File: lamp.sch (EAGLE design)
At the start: 3 parts

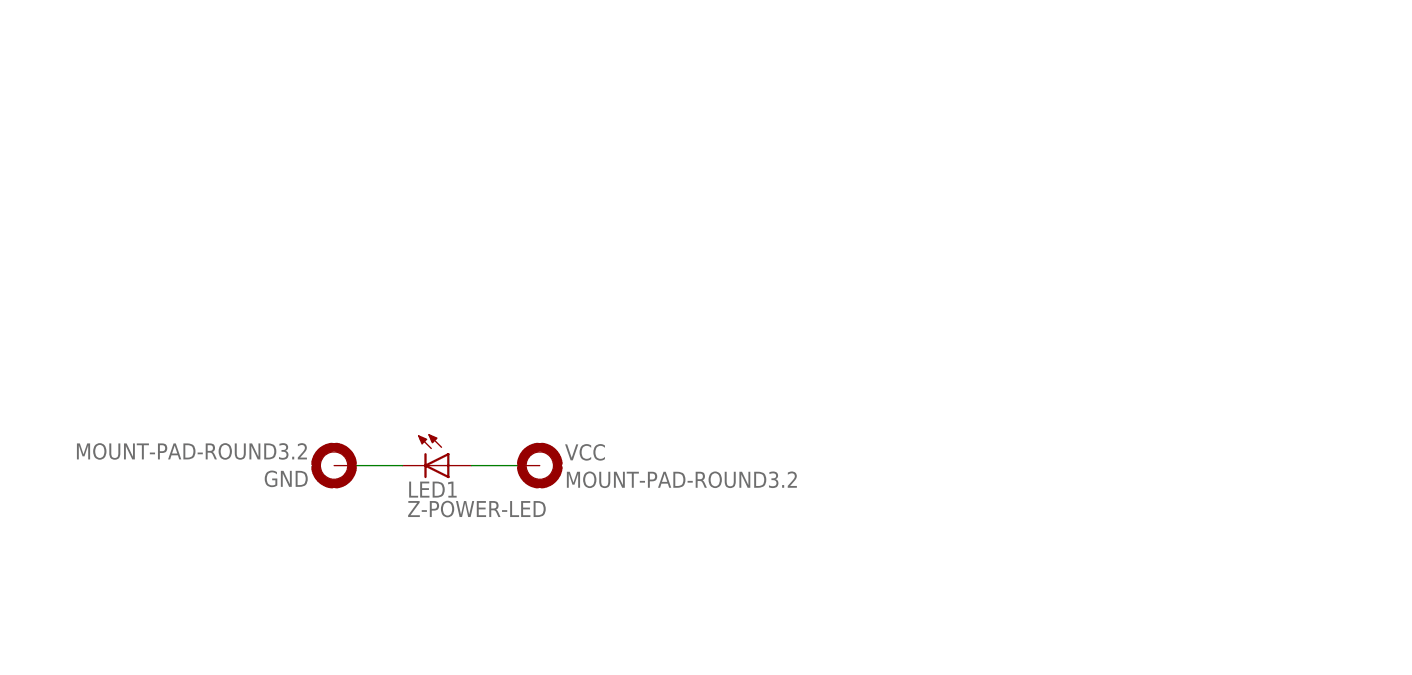
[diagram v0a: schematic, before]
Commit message: Updated the LED lamp schematic.
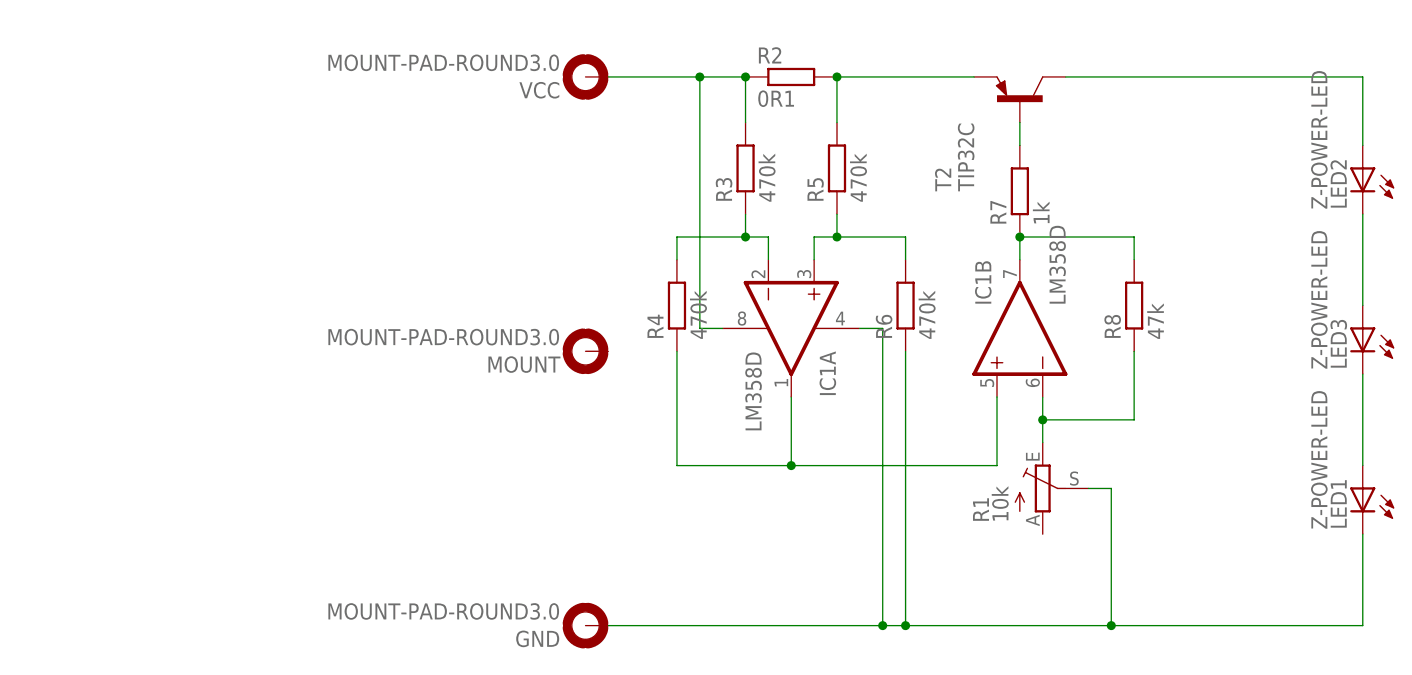
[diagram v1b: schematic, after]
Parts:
- added IC1: LM358D, linear:LM358D
- added LED2, LED3: Z-POWER-LED, led:Z-POWER-LED
- added MOUNT: MOUNT-PAD-ROUND3.0, holes:MOUNT-PAD-ROUND3.0
- added R1: 10k, pot:TRIM_EU-RJ9W
- added R2: 0R1, resistor:R-EU_0411/15
- added R3, R4, R5, R6: 470k, resistor:R-EU_M1206
- added R7: 1k, resistor:R-EU_M1206
- added R8: 47k, resistor:R-EU_M1206
- added T2: TIP32C, transistor:TIP32C
- GND, VCC: value MOUNT-PAD-ROUND3.2 -> MOUNT-PAD-ROUND3.0; device holes:MOUNT-PAD-ROUND3.2 -> holes:MOUNT-PAD-ROUND3.0
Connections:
- removed net N$1: GND.MOUNT, LED1.C
- new net GND: GND.MOUNT, IC1P.V-, LED1.C, R1.S, R6.1
- new net N$10: IC1B.-IN, R1.E, R8.1
- new net N$11: IC1A.-IN, R3.1, R4.2
- new net N$12: IC1A.+IN, R5.1, R6.2
- new net N$3: R7.2, T2.B
- new net N$4: IC1B.OUT, R7.1, R8.2
- new net N$5: LED2.A, T2.C
- new net N$6: LED2.C, LED3.A
- new net N$7: LED1.A, LED3.C
- new net N$9: IC1A.OUT, IC1B.+IN, R4.1
- new net VCC: IC1P.V+, R2.1, R3.2, VCC.MOUNT
- net N$2: now also R2.2, R5.2, T2.E; no longer LED1.A, VCC.MOUNT
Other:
- moved on the sheet: GND, LED1, VCC

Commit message: Whoops...
Swapped pins in the schematic, so gotta redo the entire PCB layout.
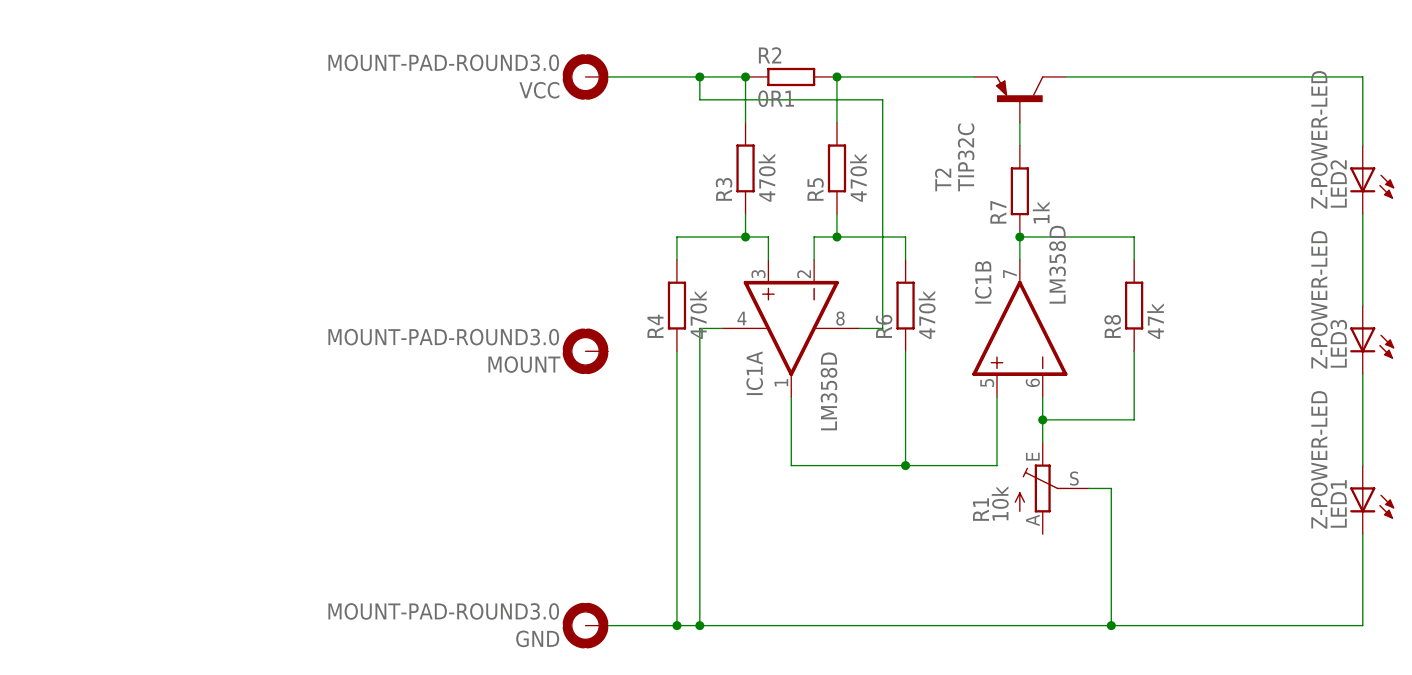
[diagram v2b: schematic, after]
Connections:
- net GND: now also R4.1; no longer R6.1
- net N$11: now also IC1A.+IN; no longer IC1A.-IN
- net N$12: now also IC1A.-IN; no longer IC1A.+IN
- net N$9: now also R6.1; no longer R4.1
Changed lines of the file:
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@@
 <grid distance="0.1" unitdist="inch" unit="inch" style="lines" multiple="1" display="no" altdistance="0.01" altunitdist="inch" altunit="inch"/>
 <layers>
-<layer number="1" name="Top" color="4" fill="1" visible="yes" active="no"/>
-<layer number="16" name="Bottom" color="1" fill="1" visible="yes" active="no"/>
-<layer number="17" name="Pads" color="2" fill="1" visible="yes" active="no"/>
-<layer number="18" name="Vias" color="2" fill="1" visible="yes" active="no"/>
-<layer number="19" name="Unrouted" color="6" fill="1" visible="yes" active="no"/>
-<layer number="20" name="Dimension" color="15" fill="1" visible="yes" active="no"/>
-<layer number="21" name="tPlace" color="7" fill="1" visible="yes" active="no"/>
-<layer number="22" name="bPlace" color="7" fill="1" visible="yes" active="no"/>
-<layer number="23" name="tOrigins" color="15" fill="1" visible="yes" active="no"/>
-<layer number="24" name="bOrigins" color="15" fill="1" visible="yes" active="no"/>
-<layer number="25" name="tNames" color="7" fill="1" visible="yes" active="no"/>
-<layer number="26" name="bNames" color="7" fill="1" visible="yes" active="no"/>
-<layer number="27" name="tValues" color="7" fill="1" visible="yes" active="no"/>
-<layer number="28" name="bValues" color="7" fill="1" visible="yes" active="no"/>
+<layer number="1" name="Top" color="4" fill="1" visible="no" active="no"/>
+<layer number="16" name="Bottom" color="1" fill="1" visible="no" active="no"/>
+<layer number="17" name="Pads" color="2" fill="1" visible="no" active="no"/>
+<layer number="18" name="Vias" color="2" fill="1" visible="no" active="no"/>
+<layer number="19" name="Unrouted" color="6" fill="1" visible="no" active="no"/>
+<layer number="20" name="Dimension" color="15" fill="1" visible="no" active="no"/>
+<layer number="21" name="tPlace" color="7" fill="1" visible="no" active="no"/>
+<layer number="22" name="bPlace" color="7" fill="1" visible="no" active="no"/>
+<layer number="23" name="tOrigins" color="15" fill="1" visible="no" active="no"/>
+<layer number="24" name="bOrigins" color="15" fill="1" visible="no" active="no"/>
+<layer number="25" name="tNames" color="7" fill="1" visible="no" active="no"/>
+<layer number="26" name="bNames" color="7" fill="1" visible="no" active="no"/>
+<layer number="27" name="tValues" color="7" fill="1" visible="no" active="no"/>
+<layer number="28" name="bValues" color="7" fill="1" visible="no" active="no"/>
 <layer number="29" name="tStop" color="7" fill="3" visible="no" active="no"/>
 <layer number="30" name="bStop" color="7" fill="6" visible="no" active="no"/>
@@
 <layer number="35" name="tGlue" color="7" fill="4" visible="no" active="no"/>
 <layer number="36" name="bGlue" color="7" fill="5" visible="no" active="no"/>
-<layer number="37" name="tTest" color="7" fill="1" visible="yes" active="no"/>
-<layer number="38" name="bTest" color="7" fill="1" visible="yes" active="no"/>
+<layer number="37" name="tTest" color="7" fill="1" visible="no" active="no"/>
+<layer number="38" name="bTest" color="7" fill="1" visible="no" active="no"/>
 <layer number="39" name="tKeepout" color="4" fill="11" visible="no" active="no"/>
 <layer number="40" name="bKeepout" color="1" fill="11" visible="no" active="no"/>
@@
 <layer number="44" name="Drills" color="7" fill="1" visible="no" active="no"/>
 <layer number="45" name="Holes" color="7" fill="1" visible="no" active="no"/>
-<layer number="46" name="Milling" color="3" fill="1" visible="yes" active="no"/>
-<layer number="47" name="Measures" color="7" fill="1" visible="yes" active="no"/>
-<layer number="48" name="Document" color="7" fill="1" visible="yes" active="no"/>
-<layer number="49" name="Reference" color="7" fill="1" visible="yes" active="no"/>
-<layer number="51" name="tDocu" color="7" fill="1" visible="yes" active="no"/>
-<layer number="52" name="bDocu" color="7" fill="1" visible="yes" active="no"/>
+<layer number="46" name="Milling" color="3" fill="1" visible="no" active="no"/>
+<layer number="47" name="Measures" color="7" fill="1" visible="no" active="no"/>
+<layer number="48" name="Document" color="7" fill="1" visible="no" active="no"/>
+<layer number="49" name="Reference" color="7" fill="1" visible="no" active="no"/>
+<layer number="51" name="tDocu" color="7" fill="1" visible="no" active="no"/>
+<layer number="52" name="bDocu" color="7" fill="1" visible="no" active="no"/>
 <layer number="91" name="Nets" color="2" fill="1" visible="yes" active="yes"/>
 <layer number="92" name="Busses" color="1" fill="1" visible="yes" active="yes"/>
@@
 <instances>
 <instance part="LED1" gate="G$1" x="81.28" y="48.26" rot="MR0"/>
-<instance part="IC1" gate="A" x="17.78" y="66.04" rot="R270"/>
+<instance part="IC1" gate="A" x="17.78" y="66.04" rot="MR270"/>
 <instance part="IC1" gate="B" x="43.18" y="66.04" rot="R90"/>
 <instance part="R1" gate="1" x="45.72" y="48.26"/>
@@
 <instance part="GND" gate="G$1" x="-5.08" y="33.02" rot="R180"/>
 <instance part="MOUNT" gate="G$1" x="-5.08" y="63.5" rot="R180"/>
-<instance part="IC1" gate="P" x="17.78" y="66.04" rot="R90"/>
+<instance part="IC1" gate="P" x="17.78" y="66.04" rot="MR90"/>
 </instances>
 <busses>
@@
 <wire x1="12.7" y1="93.98" x2="12.7" y2="88.9" width="0.1524" layer="91"/>
 <junction x="12.7" y="93.98"/>
-<wire x1="7.62" y1="93.98" x2="7.62" y2="66.04" width="0.1524" layer="91"/>
 <pinref part="IC1" gate="P" pin="V+"/>
-<wire x1="7.62" y1="66.04" x2="10.16" y2="66.04" width="0.1524" layer="91"/>
+<wire x1="25.4" y1="66.04" x2="27.94" y2="66.04" width="0.1524" layer="91"/>
+<wire x1="27.94" y1="66.04" x2="27.94" y2="91.44" width="0.1524" layer="91"/>
+<wire x1="27.94" y1="91.44" x2="7.62" y2="91.44" width="0.1524" layer="91"/>
+<wire x1="7.62" y1="91.44" x2="7.62" y2="93.98" width="0.1524" layer="91"/>
 <junction x="7.62" y="93.98"/>
 </segment>
@@
 <pinref part="GND" gate="G$1" pin="MOUNT"/>
 <pinref part="R1" gate="1" pin="S"/>
-<wire x1="53.34" y1="33.02" x2="30.48" y2="33.02" width="0.1524" layer="91"/>
-<wire x1="30.48" y1="33.02" x2="27.94" y2="33.02" width="0.1524" layer="91"/>
-<wire x1="27.94" y1="33.02" x2="-2.54" y2="33.02" width="0.1524" layer="91"/>
+<wire x1="53.34" y1="33.02" x2="7.62" y2="33.02" width="0.1524" layer="91"/>
+<wire x1="7.62" y1="33.02" x2="5.08" y2="33.02" width="0.1524" layer="91"/>
+<wire x1="5.08" y1="33.02" x2="-2.54" y2="33.02" width="0.1524" layer="91"/>
 <wire x1="50.8" y1="48.26" x2="53.34" y2="48.26" width="0.1524" layer="91"/>
 <wire x1="53.34" y1="48.26" x2="53.34" y2="33.02" width="0.1524" layer="91"/>
-<pinref part="R6" gate="G$1" pin="1"/>
-<wire x1="30.48" y1="63.5" x2="30.48" y2="33.02" width="0.1524" layer="91"/>
 <junction x="53.34" y="33.02"/>
-<junction x="30.48" y="33.02"/>
 <pinref part="IC1" gate="P" pin="V-"/>
-<wire x1="25.4" y1="66.04" x2="27.94" y2="66.04" width="0.1524" layer="91"/>
-<wire x1="27.94" y1="66.04" x2="27.94" y2="33.02" width="0.1524" layer="91"/>
-<junction x="27.94" y="33.02"/>
+<wire x1="10.16" y1="66.04" x2="7.62" y2="66.04" width="0.1524" layer="91"/>
+<wire x1="7.62" y1="66.04" x2="7.62" y2="33.02" width="0.1524" layer="91"/>
+<junction x="7.62" y="33.02"/>
+<pinref part="R4" gate="G$1" pin="1"/>
+<wire x1="5.08" y1="63.5" x2="5.08" y2="33.02" width="0.1524" layer="91"/>
+<junction x="5.08" y="33.02"/>
 </segment>
 </net>
@@
 <wire x1="17.78" y1="58.42" x2="17.78" y2="50.8" width="0.1524" layer="91"/>
 <pinref part="IC1" gate="B" pin="+IN"/>
-<wire x1="17.78" y1="50.8" x2="40.64" y2="50.8" width="0.1524" layer="91"/>
+<wire x1="17.78" y1="50.8" x2="30.48" y2="50.8" width="0.1524" layer="91"/>
+<wire x1="30.48" y1="50.8" x2="40.64" y2="50.8" width="0.1524" layer="91"/>
 <wire x1="40.64" y1="50.8" x2="40.64" y2="58.42" width="0.1524" layer="91"/>
-<pinref part="R4" gate="G$1" pin="1"/>
-<wire x1="5.08" y1="63.5" x2="5.08" y2="50.8" width="0.1524" layer="91"/>
-<wire x1="5.08" y1="50.8" x2="17.78" y2="50.8" width="0.1524" layer="91"/>
-<junction x="17.78" y="50.8"/>
+<pinref part="R6" gate="G$1" pin="1"/>
+<wire x1="30.48" y1="63.5" x2="30.48" y2="50.8" width="0.1524" layer="91"/>
+<junction x="30.48" y="50.8"/>
 </segment>
 </net>
@@
 <pinref part="R3" gate="G$1" pin="1"/>
 <wire x1="12.7" y1="78.74" x2="12.7" y2="76.2" width="0.1524" layer="91"/>
-<pinref part="IC1" gate="A" pin="-IN"/>
 <wire x1="12.7" y1="76.2" x2="15.24" y2="76.2" width="0.1524" layer="91"/>
-<wire x1="15.24" y1="76.2" x2="15.24" y2="73.66" width="0.1524" layer="91"/>
 <pinref part="R4" gate="G$1" pin="2"/>
 <wire x1="12.7" y1="76.2" x2="5.08" y2="76.2" width="0.1524" layer="91"/>
 <wire x1="5.08" y1="76.2" x2="5.08" y2="73.66" width="0.1524" layer="91"/>
 <junction x="12.7" y="76.2"/>
+<pinref part="IC1" gate="A" pin="+IN"/>
+<wire x1="15.24" y1="76.2" x2="15.24" y2="73.66" width="0.1524" layer="91"/>
 </segment>
 </net>
@@
 <pinref part="R5" gate="G$1" pin="1"/>
 <wire x1="22.86" y1="78.74" x2="22.86" y2="76.2" width="0.1524" layer="91"/>
-<pinref part="IC1" gate="A" pin="+IN"/>
 <wire x1="22.86" y1="76.2" x2="20.32" y2="76.2" width="0.1524" layer="91"/>
-<wire x1="20.32" y1="76.2" x2="20.32" y2="73.66" width="0.1524" layer="91"/>
 <pinref part="R6" gate="G$1" pin="2"/>
 <wire x1="22.86" y1="76.2" x2="30.48" y2="76.2" width="0.1524" layer="91"/>
 <wire x1="30.48" y1="76.2" x2="30.48" y2="73.66" width="0.1524" layer="91"/>
 <junction x="22.86" y="76.2"/>
-</segment>
-</net>
+<pinref part="IC1" gate="A" pin="-IN"/>
+<wire x1="20.32" y1="76.2" x2="20.32" y2="73.66" width="0.1524" layer="91"/>
+</segment>
+</net>

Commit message: Improved the design.
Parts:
- removed MOUNT: MOUNT-PAD-ROUND3.0, holes:MOUNT-PAD-ROUND3.0
- R2: device resistor:R-EU_0411/15 -> resistor:R-EU_0617/17
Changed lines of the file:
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@@
 <grid distance="0.1" unitdist="inch" unit="inch" style="lines" multiple="1" display="no" altdistance="0.01" altunitdist="inch" altunit="inch"/>
 <layers>
-<layer number="1" name="Top" color="4" fill="1" visible="no" active="no"/>
-<layer number="16" name="Bottom" color="1" fill="1" visible="no" active="no"/>
-<layer number="17" name="Pads" color="2" fill="1" visible="no" active="no"/>
-<layer number="18" name="Vias" color="2" fill="1" visible="no" active="no"/>
-<layer number="19" name="Unrouted" color="6" fill="1" visible="no" active="no"/>
-<layer number="20" name="Dimension" color="15" fill="1" visible="no" active="no"/>
-<layer number="21" name="tPlace" color="7" fill="1" visible="no" active="no"/>
-<layer number="22" name="bPlace" color="7" fill="1" visible="no" active="no"/>
-<layer number="23" name="tOrigins" color="15" fill="1" visible="no" active="no"/>
-<layer number="24" name="bOrigins" color="15" fill="1" visible="no" active="no"/>
-<layer number="25" name="tNames" color="7" fill="1" visible="no" active="no"/>
-<layer number="26" name="bNames" color="7" fill="1" visible="no" active="no"/>
-<layer number="27" name="tValues" color="7" fill="1" visible="no" active="no"/>
-<layer number="28" name="bValues" color="7" fill="1" visible="no" active="no"/>
+<layer number="1" name="Top" color="4" fill="1" visible="yes" active="no"/>
+<layer number="16" name="Bottom" color="1" fill="1" visible="yes" active="no"/>
+<layer number="17" name="Pads" color="2" fill="1" visible="yes" active="no"/>
+<layer number="18" name="Vias" color="2" fill="1" visible="yes" active="no"/>
+<layer number="19" name="Unrouted" color="6" fill="1" visible="yes" active="no"/>
+<layer number="20" name="Dimension" color="15" fill="1" visible="yes" active="no"/>
+<layer number="21" name="tPlace" color="7" fill="1" visible="yes" active="no"/>
+<layer number="22" name="bPlace" color="7" fill="1" visible="yes" active="no"/>
+<layer number="23" name="tOrigins" color="15" fill="1" visible="yes" active="no"/>
+<layer number="24" name="bOrigins" color="15" fill="1" visible="yes" active="no"/>
+<layer number="25" name="tNames" color="7" fill="1" visible="yes" active="no"/>
+<layer number="26" name="bNames" color="7" fill="1" visible="yes" active="no"/>
+<layer number="27" name="tValues" color="7" fill="1" visible="yes" active="no"/>
+<layer number="28" name="bValues" color="7" fill="1" visible="yes" active="no"/>
 <layer number="29" name="tStop" color="7" fill="3" visible="no" active="no"/>
 <layer number="30" name="bStop" color="7" fill="6" visible="no" active="no"/>
@@
 <layer number="35" name="tGlue" color="7" fill="4" visible="no" active="no"/>
 <layer number="36" name="bGlue" color="7" fill="5" visible="no" active="no"/>
-<layer number="37" name="tTest" color="7" fill="1" visible="no" active="no"/>
-<layer number="38" name="bTest" color="7" fill="1" visible="no" active="no"/>
+<layer number="37" name="tTest" color="7" fill="1" visible="yes" active="no"/>
+<layer number="38" name="bTest" color="7" fill="1" visible="yes" active="no"/>
 <layer number="39" name="tKeepout" color="4" fill="11" visible="no" active="no"/>
 <layer number="40" name="bKeepout" color="1" fill="11" visible="no" active="no"/>
@@
 <layer number="44" name="Drills" color="7" fill="1" visible="no" active="no"/>
 <layer number="45" name="Holes" color="7" fill="1" visible="no" active="no"/>
-<layer number="46" name="Milling" color="3" fill="1" visible="no" active="no"/>
-<layer number="47" name="Measures" color="7" fill="1" visible="no" active="no"/>
-<layer number="48" name="Document" color="7" fill="1" visible="no" active="no"/>
-<layer number="49" name="Reference" color="7" fill="1" visible="no" active="no"/>
-<layer number="51" name="tDocu" color="7" fill="1" visible="no" active="no"/>
-<layer number="52" name="bDocu" color="7" fill="1" visible="no" active="no"/>
+<layer number="46" name="Milling" color="3" fill="1" visible="yes" active="no"/>
+<layer number="47" name="Measures" color="7" fill="1" visible="yes" active="no"/>
+<layer number="48" name="Document" color="7" fill="1" visible="yes" active="no"/>
+<layer number="49" name="Reference" color="7" fill="1" visible="yes" active="no"/>
+<layer number="51" name="tDocu" color="7" fill="1" visible="yes" active="no"/>
+<layer number="52" name="bDocu" color="7" fill="1" visible="yes" active="no"/>
 <layer number="91" name="Nets" color="2" fill="1" visible="yes" active="yes"/>
 <layer number="92" name="Busses" color="1" fill="1" visible="yes" active="yes"/>
@@
 <part name="IC1" library="linear" deviceset="LM358" device="D" value="LM358D"/>
 <part name="R1" library="pot" deviceset="TRIM_EU-" device="RJ9W" value="10k"/>
-<part name="R2" library="resistor" deviceset="R-EU_" device="0411/15" value="0R1"/>
+<part name="R2" library="resistor" deviceset="R-EU_" device="0617/17" value="0R1"/>
 <part name="R3" library="resistor" deviceset="R-EU_" device="M1206" value="470k"/>
 <part name="R4" library="resistor" deviceset="R-EU_" device="M1206" value="470k"/>
@@
 <part name="VCC" library="holes" deviceset="MOUNT-PAD-ROUND" device="3.0"/>
 <part name="GND" library="holes" deviceset="MOUNT-PAD-ROUND" device="3.0"/>
-<part name="MOUNT" library="holes" deviceset="MOUNT-PAD-ROUND" device="3.0"/>
 </parts>
 <sheets>
@@
 <instance part="VCC" gate="G$1" x="-5.08" y="93.98" rot="R180"/>
 <instance part="GND" gate="G$1" x="-5.08" y="33.02" rot="R180"/>
-<instance part="MOUNT" gate="G$1" x="-5.08" y="63.5" rot="R180"/>
 <instance part="IC1" gate="P" x="17.78" y="66.04" rot="MR90"/>
 </instances>
